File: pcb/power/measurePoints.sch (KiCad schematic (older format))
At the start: 9 parts

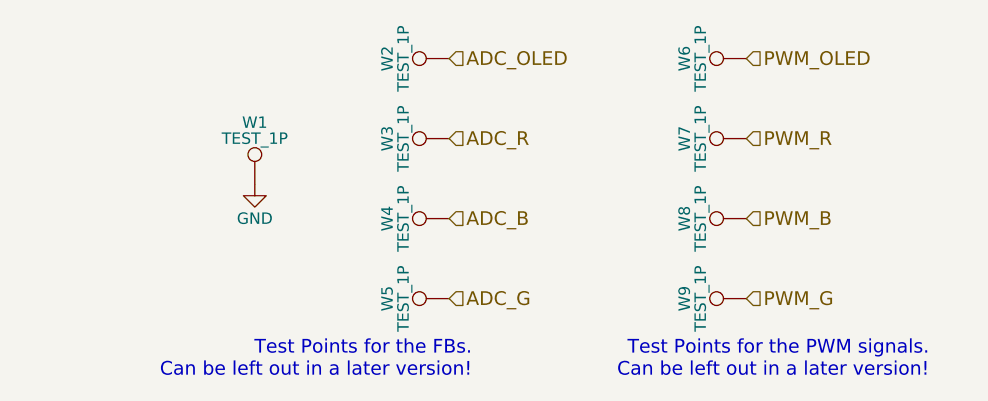
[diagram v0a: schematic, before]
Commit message: Started placing some components.
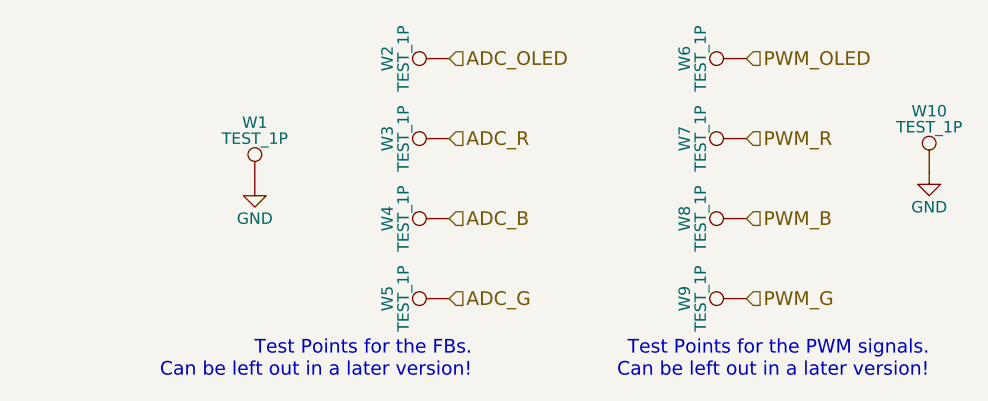
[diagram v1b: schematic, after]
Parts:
- added W10: TEST_1P, Additional:GND_PROBE, symbol TEST_1P
- W1: footprint Measurement_Points:Measurement_Point_Round-SMD-Pad_Big -> Additional:GND_PROBE
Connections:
- net GND: now also W10.1
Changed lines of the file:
@@
 F 0 "W1" H 4250 3770 50  0000 C CNN
 F 1 "TEST_1P" H 4250 3700 50  0000 C CNN
-F 2 "Measurement_Points:Measurement_Point_Round-SMD-Pad_Big" H 4450 3500 50  0001 C CNN
+F 2 "Additional:GND_PROBE" H 4450 3500 50  0001 C CNN
 F 3 "" H 4450 3500 50  0000 C CNN
 	1    4250 3500
@@
 Text HLabel 6400 4000 2    60   Input ~ 0
 PWM_G
+$Comp
+L TEST_1P W10
+U 1 1 58476E23
+P 7200 3450
+F 0 "W10" H 7200 3720 50  0000 C CNN
+F 1 "TEST_1P" H 7200 3650 50  0000 C CNN
+F 2 "Additional:GND_PROBE" H 7400 3450 50  0001 C CNN
+F 3 "" H 7400 3450 50  0000 C CNN
+	1    7200 3450
+	1    0    0    -1
+$EndComp
+$Comp
+L GND #PWR014
+U 1 1 58476E29
+P 7200 3450
+F 0 "#PWR014" H 7200 3200 50  0001 C CNN
+F 1 "GND" H 7200 3300 50  0000 C CNN
+F 2 "" H 7200 3450 50  0000 C CNN
+F 3 "" H 7200 3450 50  0000 C CNN
+	1    7200 3450
+	1    0    0    -1
+$EndComp
 $EndSCHEMATC

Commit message: Finished layout.
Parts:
- renumbered W5 to W4, W4 to W5, W9 to W8, W8 to W9
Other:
- moved on the sheet: W4, W5, W8, W9
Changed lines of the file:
@@
 $EndDescr
 $Comp
+L TEST_1P W8
+U 1 1 584302F8
+P 6400 3650
+F 0 "W8" H 6400 3920 50  0000 C CNN
+F 1 "TEST_1P" H 6400 3850 50  0000 C CNN
+F 2 "Additional:TP_PROBE" H 6600 3650 50  0001 C CNN
+F 3 "" H 6600 3650 50  0000 C CNN
+	1    6400 3650
+	0    -1   -1   0
+$EndComp
+$Comp
 L TEST_1P W9
-U 1 1 584302F8
+U 1 1 584302FF
 P 6400 4000
 F 0 "W9" H 6400 4270 50  0000 C CNN
@@
 F 3 "" H 6600 4000 50  0000 C CNN
 	1    6400 4000
-	0    -1   -1   0
-$EndComp
-$Comp
-L TEST_1P W8
-U 1 1 584302FF
-P 6400 3650
-F 0 "W8" H 6400 3920 50  0000 C CNN
-F 1 "TEST_1P" H 6400 3850 50  0000 C CNN
-F 2 "Additional:TP_PROBE" H 6600 3650 50  0001 C CNN
-F 3 "" H 6600 3650 50  0000 C CNN
-	1    6400 3650
 	0    -1   -1   0
 $EndComp
@@
 $EndComp
 $Comp
+L TEST_1P W4
+U 1 1 58430314
+P 5100 3650
+F 0 "W4" H 5100 3920 50  0000 C CNN
+F 1 "TEST_1P" H 5100 3850 50  0000 C CNN
+F 2 "Additional:TP_PROBE" H 5300 3650 50  0001 C CNN
+F 3 "" H 5300 3650 50  0000 C CNN
+	1    5100 3650
+	0    -1   -1   0
+$EndComp
+$Comp
 L TEST_1P W5
-U 1 1 58430314
+U 1 1 5843031B
 P 5100 4000
 F 0 "W5" H 5100 4270 50  0000 C CNN
@@
 F 3 "" H 5300 4000 50  0000 C CNN
 	1    5100 4000
-	0    -1   -1   0
-$EndComp
-$Comp
-L TEST_1P W4
-U 1 1 5843031B
-P 5100 3650
-F 0 "W4" H 5100 3920 50  0000 C CNN
-F 1 "TEST_1P" H 5100 3850 50  0000 C CNN
-F 2 "Additional:TP_PROBE" H 5300 3650 50  0001 C CNN
-F 3 "" H 5300 3650 50  0000 C CNN
-	1    5100 3650
 	0    -1   -1   0
 $EndComp
@@
 $EndComp
 $Comp
-L GND #PWR12
+L GND #PWR1
 U 1 1 58430341
 P 4250 3500
-F 0 "#PWR12" H 4250 3250 50  0001 C CNN
+F 0 "#PWR1" H 4250 3250 50  0001 C CNN
 F 1 "GND" H 4250 3350 50  0000 C CNN
 F 2 "" H 4250 3500 50  0000 C CNN
@@
 Text HLabel 5100 3300 2    60   Input ~ 0
 ADC_R
+Text HLabel 5100 4000 2    60   Input ~ 0
+ADC_B
 Text HLabel 5100 3650 2    60   Input ~ 0
-ADC_B
-Text HLabel 5100 4000 2    60   Input ~ 0
 ADC_G
 Text HLabel 6400 2950 2    60   Input ~ 0
@@
 Text HLabel 6400 3300 2    60   Input ~ 0
 PWM_R
+Text HLabel 6400 4000 2    60   Input ~ 0
+PWM_B
 Text HLabel 6400 3650 2    60   Input ~ 0
-PWM_B
-Text HLabel 6400 4000 2    60   Input ~ 0
 PWM_G
 $Comp
@@
 $EndComp
 $Comp
-L GND #PWR13
+L GND #PWR2
 U 1 1 58476E29
 P 7200 3450
-F 0 "#PWR13" H 7200 3200 50  0001 C CNN
+F 0 "#PWR2" H 7200 3200 50  0001 C CNN
 F 1 "GND" H 7200 3300 50  0000 C CNN
 F 2 "" H 7200 3450 50  0000 C CNN

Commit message: Finished rev 1 and generated gerber files.
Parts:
- renumbered W2 to W1, W3 to W2, W4 to W3, W5 to W4, W1 to W5
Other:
- moved on the sheet: W5
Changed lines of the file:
@@
 $EndComp
 $Comp
-L TEST_1P W4
+L TEST_1P W3
 U 1 1 58430314
 P 5100 3650
-F 0 "W4" H 5100 3920 50  0000 C CNN
+F 0 "W3" H 5100 3920 50  0000 C CNN
 F 1 "TEST_1P" H 5100 3850 50  0000 C CNN
 F 2 "Additional:TP_PROBE" H 5300 3650 50  0001 C CNN
@@
 $EndComp
 $Comp
-L TEST_1P W5
+L TEST_1P W4
 U 1 1 5843031B
 P 5100 4000
-F 0 "W5" H 5100 4270 50  0000 C CNN
+F 0 "W4" H 5100 4270 50  0000 C CNN
 F 1 "TEST_1P" H 5100 4200 50  0000 C CNN
 F 2 "Additional:TP_PROBE" H 5300 4000 50  0001 C CNN
@@
 $EndComp
 $Comp
-L TEST_1P W3
+L TEST_1P W2
 U 1 1 58430322
 P 5100 3300
-F 0 "W3" H 5100 3570 50  0000 C CNN
+F 0 "W2" H 5100 3570 50  0000 C CNN
 F 1 "TEST_1P" H 5100 3500 50  0000 C CNN
 F 2 "Additional:TP_PROBE" H 5300 3300 50  0001 C CNN
@@
 $EndComp
 $Comp
-L TEST_1P W2
+L TEST_1P W1
 U 1 1 58430329
 P 5100 2950
-F 0 "W2" H 5100 3220 50  0000 C CNN
+F 0 "W1" H 5100 3220 50  0000 C CNN
 F 1 "TEST_1P" H 5100 3150 50  0000 C CNN
 F 2 "Additional:TP_PROBE" H 5300 2950 50  0001 C CNN
@@
 Test Points for the PWM signals.\nCan be left out in a later version!
 $Comp
-L TEST_1P W1
+L TEST_1P W5
 U 1 1 5843033A
-P 4250 3500
-F 0 "W1" H 4250 3770 50  0000 C CNN
-F 1 "TEST_1P" H 4250 3700 50  0000 C CNN
-F 2 "Additional:GND_PROBE" H 4450 3500 50  0001 C CNN
-F 3 "" H 4450 3500 50  0000 C CNN
-	1    4250 3500
+P 5775 3500
+F 0 "W5" H 5775 3770 50  0000 C CNN
+F 1 "TEST_1P" H 5775 3700 50  0000 C CNN
+F 2 "Additional:GND_PROBE" H 5975 3500 50  0001 C CNN
+F 3 "" H 5975 3500 50  0000 C CNN
+	1    5775 3500
 	1    0    0    -1
 $EndComp
@@
 L GND #PWR1
 U 1 1 58430341
-P 4250 3500
-F 0 "#PWR1" H 4250 3250 50  0001 C CNN
-F 1 "GND" H 4250 3350 50  0000 C CNN
-F 2 "" H 4250 3500 50  0000 C CNN
-F 3 "" H 4250 3500 50  0000 C CNN
-	1    4250 3500
+P 5775 3500
+F 0 "#PWR1" H 5775 3250 50  0001 C CNN
+F 1 "GND" H 5775 3350 50  0000 C CNN
+F 2 "" H 5775 3500 50  0000 C CNN
+F 3 "" H 5775 3500 50  0000 C CNN
+	1    5775 3500
 	1    0    0    -1
 $EndComp
